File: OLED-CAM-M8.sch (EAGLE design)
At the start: 17 parts, among them J5 U.FL

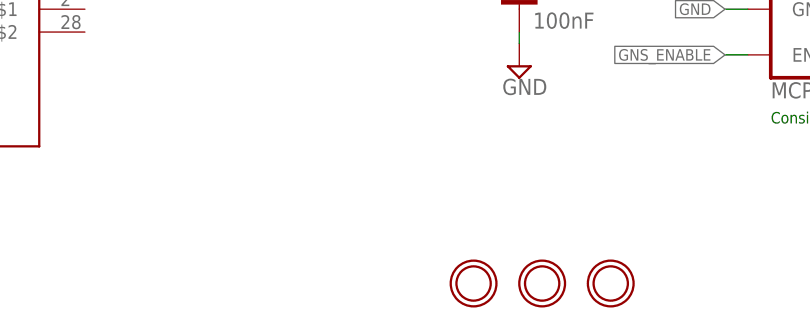
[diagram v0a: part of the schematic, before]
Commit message: Added mounting hole
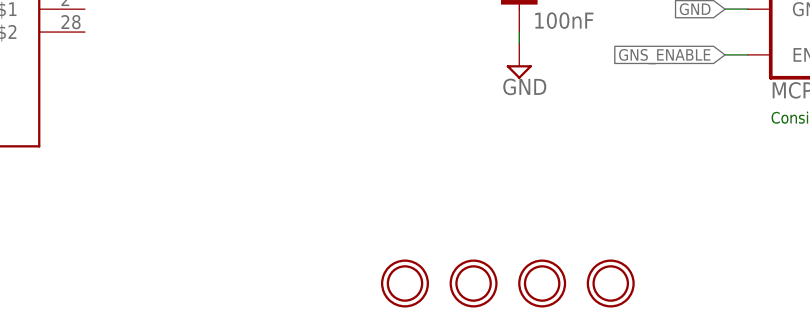
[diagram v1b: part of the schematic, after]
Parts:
- added U$1: MOUNTINGHOLE2.0, microbuilder:MOUNTINGHOLE2.0
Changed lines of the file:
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@@
 <part name="U$2" library="diy-modules" deviceset="DISPLAY-OLED-128X64-I2C" device=""/>
 <part name="J1" library="SparkFun-Connectors" library_urn="urn:adsk.eagle:library:513" deviceset="CONN_12" device="" package3d_urn="urn:adsk.eagle:package:38169/1"/>
+<part name="U$1" library="microbuilder" deviceset="MOUNTINGHOLE" device="2.0"/>
 </parts>
 <sheets>
@@
 <attribute name="NAME" x="208.28" y="168.148" size="1.778" layer="95" font="vector"/>
 </instance>
+<instance part="U$1" gate="G$1" x="147.32" y="7.62" smashed="yes"/>
 </instances>
 <busses>

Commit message: Swapped VCC GND
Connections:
- net GND: now also U$2.VCC; no longer U$2.GND
- net OLED_VCC: now also U$2.GND; no longer U$2.VCC
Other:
- note added: "GND AND VCC are reversed on the parts avaliable... Check the actual part!!!"
- note added: "R0.4"
- note removed: "R0.2"
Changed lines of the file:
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@@
 <attributes>
 <attribute name="CNAME" value="OLED-CAM-M8"/>
-<attribute name="CREVISION" value="0.2"/>
+<attribute name="CREVISION" value="0.4"/>
 <attribute name="DESIGNER" value="gregcope@gmail.com"/>
 </attributes>
@@
 <plain>
 <text x="101.6" y="162.56" size="3.048" layer="94" ratio="12">Greg Cope</text>
-<text x="189.23" y="167.64" size="3.048" layer="94" ratio="12">R0.2</text>
+<text x="189.23" y="167.64" size="3.048" layer="94" ratio="12">R0.4</text>
 <text x="101.6" y="167.64" size="4.572" layer="94" ratio="15">MoteinoM0 AboatMon Shield</text>
 <text x="187.96" y="25.4" size="1.27" layer="91">Consider MCP1810 lower shutdown current 1na</text>
 <text x="116.84" y="106.68" size="1.778" layer="91">Part: DISPLAY-OLED-128X64-I2C</text>
+<text x="121.92" y="144.78" size="1.778" layer="91">GND AND VCC are reversed on
+the parts avaliable...
+Check the actual part!!!</text>
 </plain>
 <instances>
@@
 </segment>
 <segment>
-<pinref part="U$2" gate="G$1" pin="GND"/>
-<wire x1="124.46" y1="139.7" x2="134.62" y2="139.7" width="0.1524" layer="91"/>
-<label x="134.62" y="139.7" size="1.27" layer="95" xref="yes"/>
-</segment>
-<segment>
 <pinref part="J1" gate="G$1" pin="12"/>
 <wire x1="218.44" y1="165.1" x2="228.6" y2="165.1" width="0.1524" layer="91"/>
 <label x="228.6" y="165.1" size="1.27" layer="95" xref="yes"/>
+</segment>
+<segment>
+<pinref part="U$2" gate="G$1" pin="VCC"/>
+<wire x1="124.46" y1="137.16" x2="134.62" y2="137.16" width="0.1524" layer="91"/>
+<label x="134.62" y="137.16" size="1.27" layer="95" xref="yes"/>
 </segment>
 </net>
@@
 </segment>
 <segment>
-<pinref part="U$2" gate="G$1" pin="VCC"/>
-<wire x1="124.46" y1="137.16" x2="134.62" y2="137.16" width="0.1524" layer="91"/>
-<label x="134.62" y="137.16" size="1.27" layer="95" xref="yes"/>
+<pinref part="U$2" gate="G$1" pin="GND"/>
+<wire x1="124.46" y1="139.7" x2="134.62" y2="139.7" width="0.1524" layer="91"/>
+<label x="134.62" y="139.7" size="1.27" layer="95" xref="yes"/>
 </segment>
 </net>
@@
 </drawing>
 <compatibility>
+<note version="6.3" minversion="6.2.2" severity="warning">
+Since Version 6.2.2 text objects can contain more than one line,
+which will not be processed correctly with this version.
+</note>
 <note version="8.2" severity="warning">
 Since Version 8.2, EAGLE supports online libraries. The ids

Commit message: removed mounting hole and moved 100n cap
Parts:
- removed U$1, U$9: MOUNTINGHOLE2.0, microbuilder:MOUNTINGHOLE2.0
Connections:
- removed net LNA_EN: J1.7, U$5.LNA_EN
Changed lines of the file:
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@@
 <part name="SUPPLY5" library="supply2" library_urn="urn:adsk.eagle:library:372" deviceset="GND" device=""/>
 <part name="D1" library="SparkFun-LED" library_urn="urn:adsk.eagle:library:529" deviceset="LED-GREEN" device="0603" package3d_urn="urn:adsk.eagle:package:39354/1" value="GREEN"/>
-<part name="U$9" library="microbuilder" deviceset="MOUNTINGHOLE" device="2.0"/>
 <part name="J5" library="SparkFun-Connectors" library_urn="urn:adsk.eagle:library:513" deviceset="U.FL2PIN" device="" package3d_urn="urn:adsk.eagle:package:38237/1" value="U.FL"/>
 <part name="SUPPLY1" library="supply2" library_urn="urn:adsk.eagle:library:372" deviceset="GND" device=""/>
@@
 <part name="U$2" library="diy-modules" deviceset="DISPLAY-OLED-128X64-I2C" device=""/>
 <part name="J1" library="SparkFun-Connectors" library_urn="urn:adsk.eagle:library:513" deviceset="CONN_12" device="" package3d_urn="urn:adsk.eagle:package:38169/1"/>
-<part name="U$1" library="microbuilder" deviceset="MOUNTINGHOLE" device="2.0"/>
 </parts>
 <sheets>
@@
 <attribute name="VALUE" x="30.988" y="43.815" size="1.778" layer="96" font="vector" align="top-left"/>
 </instance>
-<instance part="U$9" gate="G$1" x="154.94" y="7.62" smashed="yes"/>
 <instance part="J5" gate="G$1" x="157.48" y="63.5" smashed="yes">
 <attribute name="NAME" x="154.94" y="58.42" size="1.778" layer="95" rot="R90"/>
@@
 <attribute name="NAME" x="208.28" y="168.148" size="1.778" layer="95" font="vector"/>
 </instance>
-<instance part="U$1" gate="G$1" x="147.32" y="7.62" smashed="yes"/>
 </instances>
 <busses>
@@
 </segment>
 </net>
-<net name="LNA_EN" class="2">
-<segment>
-<pinref part="U$5" gate="G$1" pin="LNA_EN"/>
-<wire x1="111.76" y1="50.8" x2="121.92" y2="50.8" width="0.1524" layer="91"/>
-<label x="121.92" y="50.8" size="1.27" layer="95" xref="yes"/>
-</segment>
-<segment>
-<pinref part="J1" gate="G$1" pin="7"/>
-<wire x1="218.44" y1="152.4" x2="228.6" y2="152.4" width="0.1524" layer="91"/>
-<label x="228.6" y="152.4" size="1.27" layer="95" xref="yes"/>
-</segment>
-</net>

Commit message: Moved 3v rail
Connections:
- net 3.3V: now also J1.7; no longer J1.4
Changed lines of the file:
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@@
 <clearance class="1" value="0.4064"/>
 </class>
-<class number="2" name="gns" width="0.4064" drill="0">
-<clearance class="2" value="0.4064"/>
+<class number="2" name="gns" width="0.3048" drill="0">
+<clearance class="2" value="0.3048"/>
 </class>
 </classes>
@@
 </segment>
 <segment>
-<wire x1="218.44" y1="144.78" x2="228.6" y2="144.78" width="0.1524" layer="91"/>
-<label x="228.6" y="144.78" size="1.27" layer="95" xref="yes"/>
-<pinref part="J1" gate="G$1" pin="4"/>
+<pinref part="J1" gate="G$1" pin="7"/>
+<wire x1="218.44" y1="152.4" x2="228.6" y2="152.4" width="0.1524" layer="91"/>
+<label x="228.6" y="152.4" size="1.27" layer="95" xref="yes"/>
 </segment>
 </net>

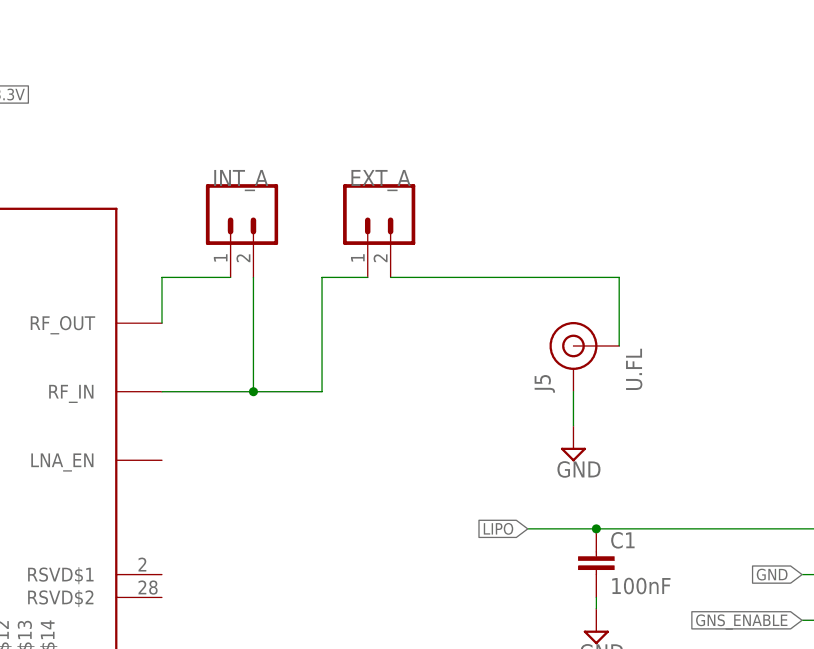
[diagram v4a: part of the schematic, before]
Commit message: removed ufl and jumpers
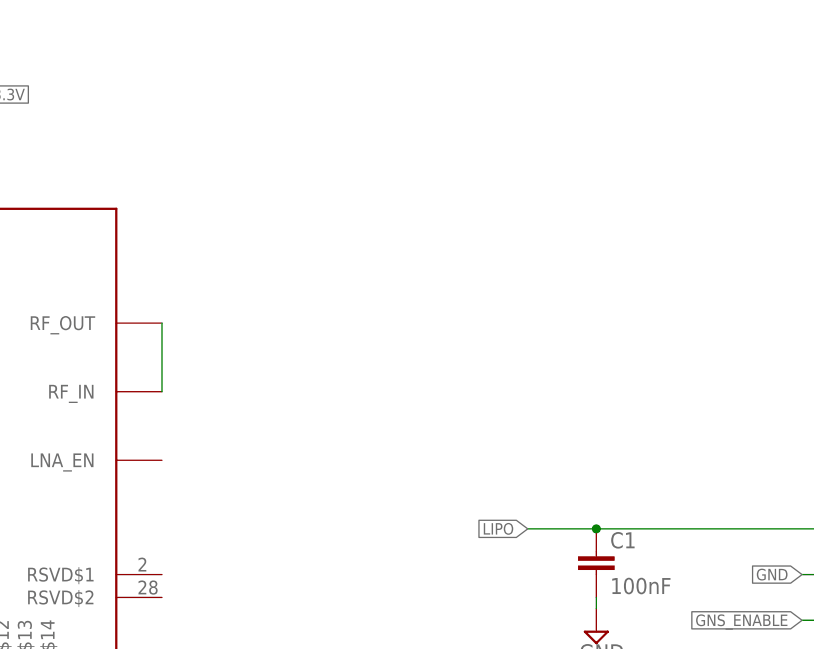
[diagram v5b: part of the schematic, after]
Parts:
- removed EXT_A, INT_A: (no value), SparkFun-Connectors:CONN_02
- removed J5: U.FL, SparkFun-Connectors:U.FL2PIN
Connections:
- removed net N$6: EXT_A.2, J5.SIGNAL
- removed net N$7: INT_A.1, U$5.RF_OUT
- net GND: no longer J5.GND
- net N$5: now also U$5.RF_OUT; no longer EXT_A.1, INT_A.2
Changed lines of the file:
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@@
 <part name="SUPPLY5" library="supply2" library_urn="urn:adsk.eagle:library:372" deviceset="GND" device=""/>
 <part name="D1" library="SparkFun-LED" library_urn="urn:adsk.eagle:library:529" deviceset="LED-GREEN" device="0603" package3d_urn="urn:adsk.eagle:package:39354/1" value="GREEN"/>
-<part name="J5" library="SparkFun-Connectors" library_urn="urn:adsk.eagle:library:513" deviceset="U.FL2PIN" device="" package3d_urn="urn:adsk.eagle:package:38237/1" value="U.FL"/>
-<part name="SUPPLY1" library="supply2" library_urn="urn:adsk.eagle:library:372" deviceset="GND" device=""/>
-<part name="INT_A" library="SparkFun-Connectors" library_urn="urn:adsk.eagle:library:513" deviceset="CONN_02" device="" package3d_urn="urn:adsk.eagle:package:38039/1"/>
-<part name="EXT_A" library="SparkFun-Connectors" library_urn="urn:adsk.eagle:library:513" deviceset="CONN_02" device="" package3d_urn="urn:adsk.eagle:package:38039/1"/>
 <part name="U$2" library="diy-modules" deviceset="DISPLAY-OLED-128X64-I2C" device=""/>
 <part name="J1" library="SparkFun-Connectors" library_urn="urn:adsk.eagle:library:513" deviceset="CONN_12" device="" package3d_urn="urn:adsk.eagle:package:38169/1"/>
@@
 <attribute name="NAME" x="30.988" y="49.149" size="1.778" layer="95" font="vector"/>
 <attribute name="VALUE" x="30.988" y="43.815" size="1.778" layer="96" font="vector" align="top-left"/>
-</instance>
-<instance part="J5" gate="G$1" x="157.48" y="63.5" smashed="yes">
-<attribute name="NAME" x="154.94" y="58.42" size="1.778" layer="95" rot="R90"/>
-<attribute name="VALUE" x="165.1" y="58.42" size="1.778" layer="96" rot="R90"/>
-</instance>
-<instance part="SUPPLY1" gate="GND" x="157.48" y="52.07" smashed="yes">
-<attribute name="VALUE" x="155.575" y="48.895" size="1.778" layer="96"/>
-</instance>
-<instance part="INT_A" gate="G$1" x="119.38" y="78.74" smashed="yes" rot="R270">
-<attribute name="VALUE" x="114.554" y="81.28" size="1.778" layer="96" font="vector" rot="R270"/>
-<attribute name="NAME" x="117.348" y="81.28" size="1.778" layer="95" font="vector"/>
-</instance>
-<instance part="EXT_A" gate="G$1" x="134.62" y="78.74" smashed="yes" rot="R270">
-<attribute name="VALUE" x="129.794" y="81.28" size="1.778" layer="96" font="vector" rot="R270"/>
-<attribute name="NAME" x="132.588" y="81.28" size="1.778" layer="95" font="vector"/>
 </instance>
 <instance part="U$2" gate="G$1" x="104.14" y="134.62" smashed="yes" rot="R270">
@@
 </segment>
 <segment>
-<pinref part="J5" gate="G$1" pin="GND"/>
-<pinref part="SUPPLY1" gate="GND" pin="GND"/>
-<wire x1="157.48" y1="58.42" x2="157.48" y2="54.61" width="0.1524" layer="91"/>
-</segment>
-<segment>
 <pinref part="J1" gate="G$1" pin="12"/>
 <wire x1="218.44" y1="165.1" x2="228.6" y2="165.1" width="0.1524" layer="91"/>
@@
 </segment>
 </net>
-<net name="N$6" class="0">
-<segment>
-<pinref part="J5" gate="G$1" pin="SIGNAL"/>
-<wire x1="162.56" y1="63.5" x2="162.56" y2="71.12" width="0.1524" layer="91"/>
-<pinref part="EXT_A" gate="G$1" pin="2"/>
-<wire x1="162.56" y1="71.12" x2="137.16" y2="71.12" width="0.1524" layer="91"/>
-</segment>
-</net>
-<net name="N$5" class="2">
-<segment>
-<pinref part="EXT_A" gate="G$1" pin="1"/>
-<wire x1="134.62" y1="71.12" x2="129.54" y2="71.12" width="0.1524" layer="91"/>
-<wire x1="129.54" y1="71.12" x2="129.54" y2="58.42" width="0.1524" layer="91"/>
-<pinref part="U$5" gate="G$1" pin="RF_IN"/>
-<wire x1="129.54" y1="58.42" x2="121.92" y2="58.42" width="0.1524" layer="91"/>
-<pinref part="INT_A" gate="G$1" pin="2"/>
-<wire x1="121.92" y1="58.42" x2="111.76" y2="58.42" width="0.1524" layer="91"/>
-<wire x1="121.92" y1="71.12" x2="121.92" y2="58.42" width="0.1524" layer="91"/>
-<junction x="121.92" y="58.42"/>
-</segment>
-</net>
-<net name="N$7" class="2">
-<segment>
-<pinref part="U$5" gate="G$1" pin="RF_OUT"/>
-<pinref part="INT_A" gate="G$1" pin="1"/>
-<wire x1="111.76" y1="66.04" x2="111.76" y2="71.12" width="0.1524" layer="91"/>
-<wire x1="111.76" y1="71.12" x2="119.38" y2="71.12" width="0.1524" layer="91"/>
-</segment>
-</net>
 <net name="TIMEPULSE" class="0">
 <segment>
@@
 </segment>
 </net>
+<net name="N$5" class="0">
+<segment>
+<pinref part="U$5" gate="G$1" pin="RF_OUT"/>
+<pinref part="U$5" gate="G$1" pin="RF_IN"/>
+<wire x1="111.76" y1="66.04" x2="111.76" y2="58.42" width="0.1524" layer="91"/>
+</segment>
+</net>
